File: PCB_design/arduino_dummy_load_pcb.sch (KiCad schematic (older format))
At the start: 22 parts, among them J1 Barrel_Jack, J2 Conn_02x08_Odd_Even, U1 MCP3208

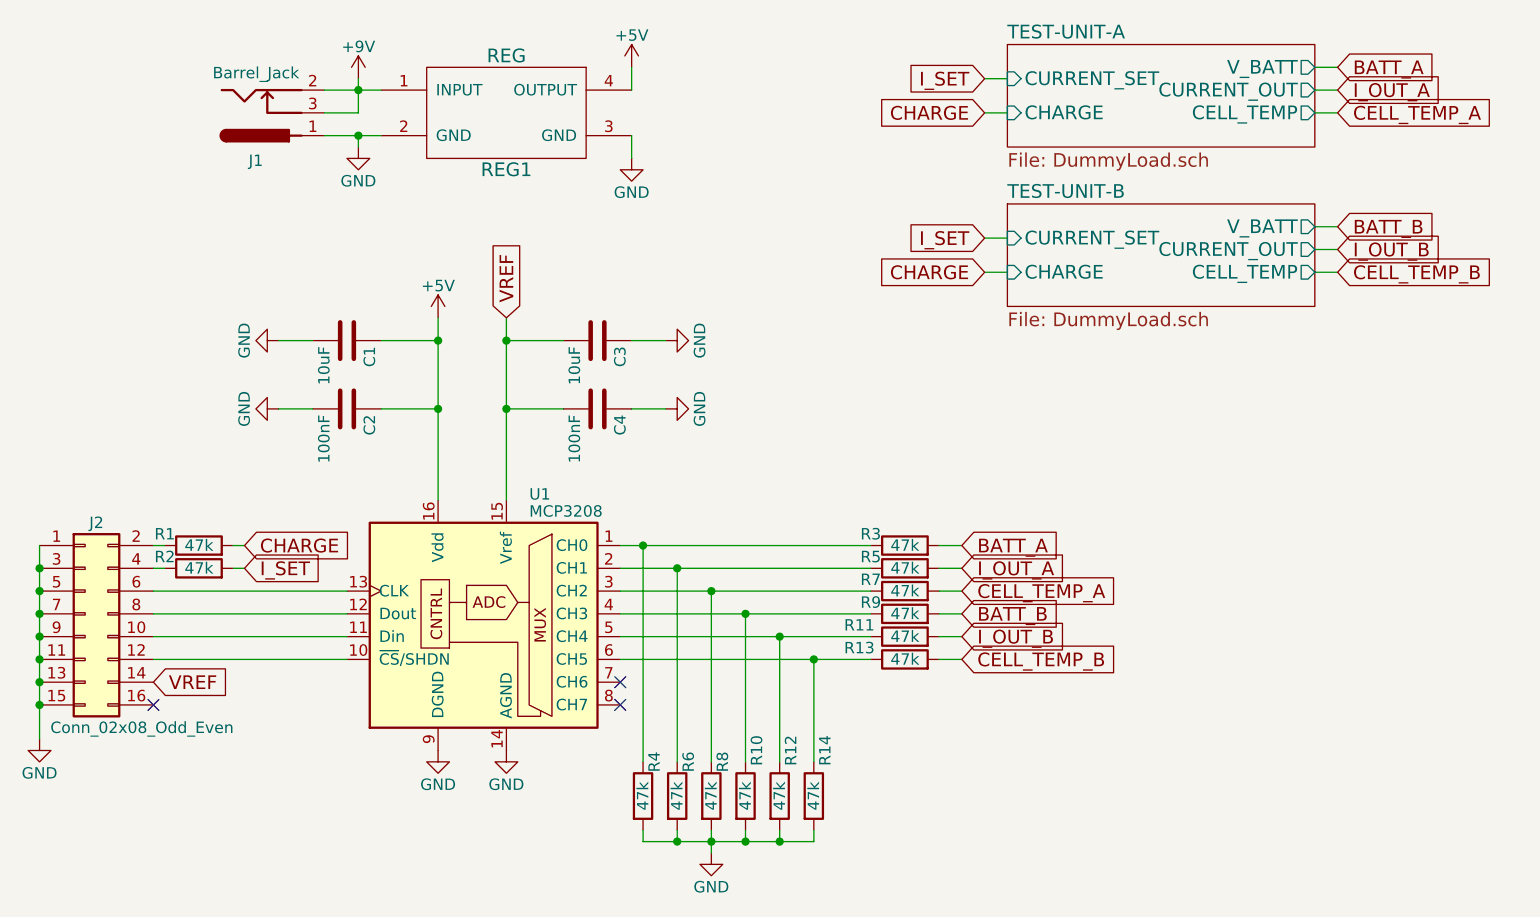
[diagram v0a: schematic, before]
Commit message: nearly finished PCB layout and routing
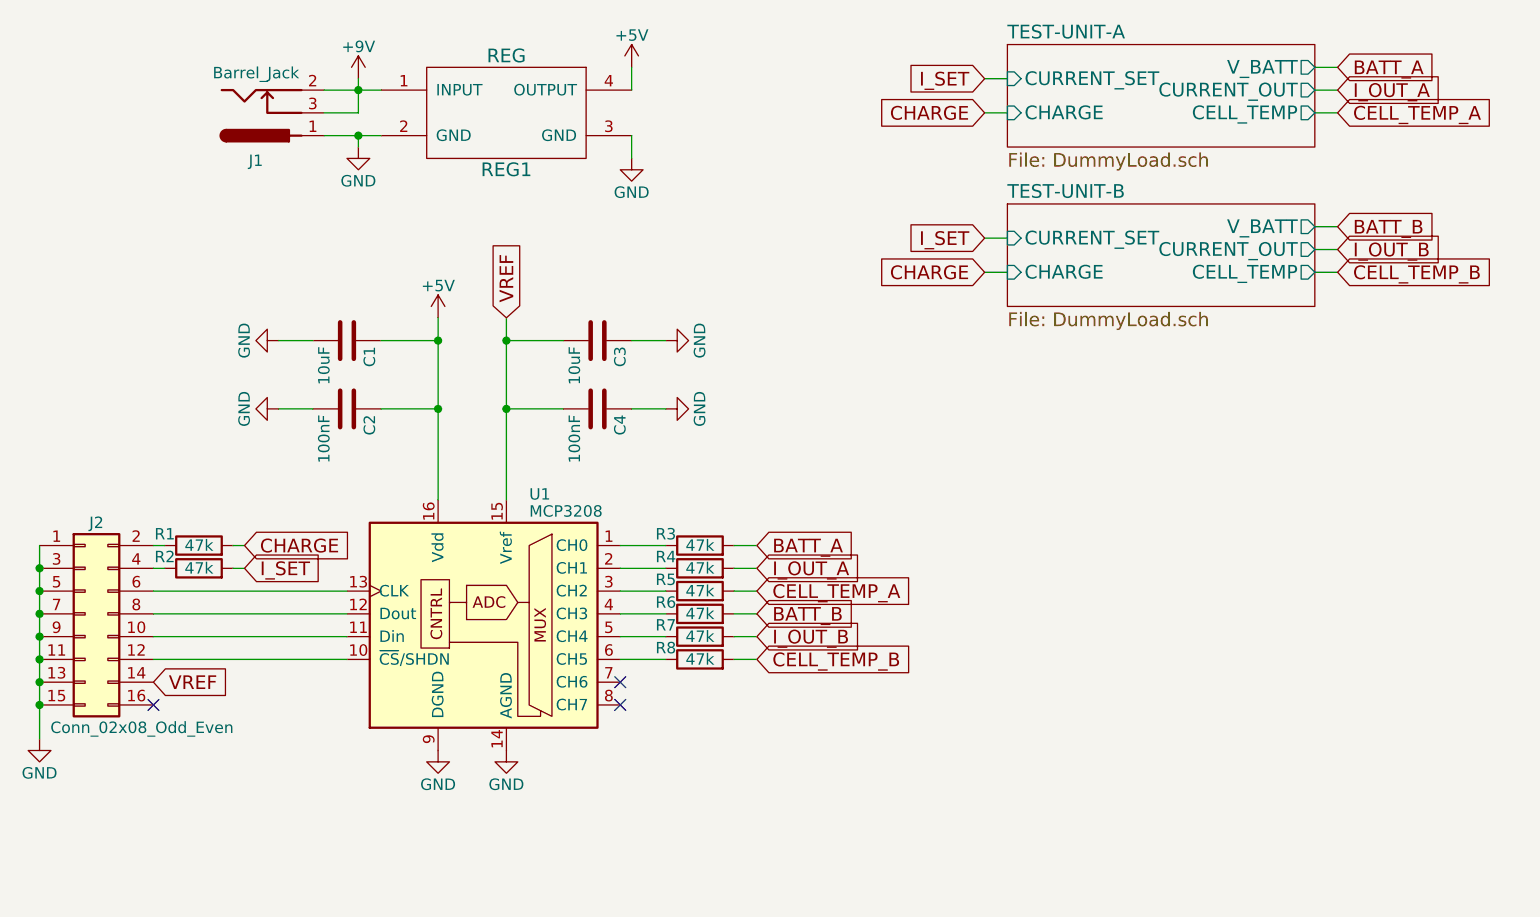
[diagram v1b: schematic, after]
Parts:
- removed R10, R11, R12, R13, R14, R9: 47k, Resistors_SMD:R_0805_HandSoldering, symbol R
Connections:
- net BATT_B: now also R6.2
- net CELL_TEMP_A: now also R5.2; no longer R7.2
- net CELL_TEMP_B: now also R8.2
- net GND: no longer R4.2, R6.2, R8.2
- net I_OUT_A: now also R4.2; no longer R5.2
- net I_OUT_B: now also R7.2
- net at R3.1, U1.1 (CH0): no longer R4.1
- net at U1.4 (CH3): now also R6.1
- net at U1.5 (CH4): now also R7.1
- net at U1.6 (CH5): now also R8.1
- new net: R4.1, U1.2 (CH1)
- new net: R5.1, U1.3 (CH2)
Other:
- moved on the sheet: R3, R4, R5, R6, R7, R8

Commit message: Finalized/finished PCB layout. Phew! Version 0.00. Hopefully it works (fingers crossed)!
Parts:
- removed R8: 47k, Resistors_SMD:R_0805_HandSoldering, symbol R
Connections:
- net BATT_B: now also R5.2; no longer R6.2
- net CELL_TEMP_A: now also R4.2; no longer R5.2
- net CELL_TEMP_B: now also R7.2
- net I_OUT_A: now also U1.2 (CH1); no longer R4.2
- net I_OUT_B: now also R6.2; no longer R7.2
- net at R4.1: now also U1.3 (CH2); no longer U1.2 (CH1)
- net at R5.1: now also U1.4 (CH3); no longer U1.3 (CH2)
- net at R6.1: now also U1.5 (CH4); no longer U1.4 (CH3)
- net at R7.1: now also U1.6 (CH5); no longer U1.5 (CH4)
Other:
- moved on the sheet: R4, R5, R6, R7
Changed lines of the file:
@@
 L R R4
 U 1 1 5A216AEF
-P 4500 3250
-F 0 "R4" V 4550 3400 50  0000 C CNN
-F 1 "47k" V 4500 3250 50  0000 C CNN
-F 2 "Resistors_SMD:R_0805_HandSoldering" V 4430 3250 50  0001 C CNN
-F 3 "" H 4500 3250 50  0001 C CNN
-	1    4500 3250
-	0    -1   -1   0
-$EndComp
-Text GLabel 2500 3150 2    60   Input ~ 0
-CHARGE
-$Comp
-L R R5
-U 1 1 5A22131E
 P 4500 3350
-F 0 "R5" V 4550 3500 50  0000 C CNN
+F 0 "R4" V 4550 3500 50  0000 C CNN
 F 1 "47k" V 4500 3350 50  0000 C CNN
 F 2 "Resistors_SMD:R_0805_HandSoldering" V 4430 3350 50  0001 C CNN
@@
 	0    -1   -1   0
 $EndComp
+Text GLabel 2500 3150 2    60   Input ~ 0
+CHARGE
+$Comp
+L R R5
+U 1 1 5A22131E
+P 4500 3450
+F 0 "R5" V 4550 3600 50  0000 C CNN
+F 1 "47k" V 4500 3450 50  0000 C CNN
+F 2 "Resistors_SMD:R_0805_HandSoldering" V 4430 3450 50  0001 C CNN
+F 3 "" H 4500 3450 50  0001 C CNN
+	1    4500 3450
+	0    -1   -1   0
+$EndComp
 $Comp
 L R R7
 U 1 1 5A22951F
+P 4500 3650
+F 0 "R7" V 4550 3800 50  0000 C CNN
+F 1 "47k" V 4500 3650 50  0000 C CNN
+F 2 "Resistors_SMD:R_0805_HandSoldering" V 4430 3650 50  0001 C CNN
+F 3 "" H 4500 3650 50  0001 C CNN
+	1    4500 3650
+	0    -1   -1   0
+$EndComp
+$Comp
+L R R6
+U 1 1 5A2293D0
 P 4500 3550
-F 0 "R7" V 4550 3700 50  0000 C CNN
+F 0 "R6" V 4550 3700 50  0000 C CNN
 F 1 "47k" V 4500 3550 50  0000 C CNN
 F 2 "Resistors_SMD:R_0805_HandSoldering" V 4430 3550 50  0001 C CNN
@@
 	0    -1   -1   0
 $EndComp
-$Comp
-L R R6
-U 1 1 5A2293D0
-P 4500 3450
-F 0 "R6" V 4550 3600 50  0000 C CNN
-F 1 "47k" V 4500 3450 50  0000 C CNN
-F 2 "Resistors_SMD:R_0805_HandSoldering" V 4430 3450 50  0001 C CNN
-F 3 "" H 4500 3450 50  0001 C CNN
-	1    4500 3450
-	0    -1   -1   0
-$EndComp
 Text GLabel 4750 3350 2    60   Input ~ 0
 CELL_TEMP_A
 Text GLabel 4750 3650 2    60   Input ~ 0
 CELL_TEMP_B
-$Comp
-L R R8
-U 1 1 5A230070
-P 4500 3650
-F 0 "R8" V 4550 3800 50  0000 C CNN
-F 1 "47k" V 4500 3650 50  0000 C CNN
-F 2 "Resistors_SMD:R_0805_HandSoldering" V 4430 3650 50  0001 C CNN
-F 3 "" H 4500 3650 50  0001 C CNN
-	1    4500 3650
-	0    -1   -1   0
-$EndComp
 $Comp
 L Conn_02x08_Odd_Even J2
@@
 $EndComp
 $Comp
-L +5V #PWR07
+L +5V #PWR06
 U 1 1 59F7FE3E
 P 3350 2150
-F 0 "#PWR07" H 3350 2000 50  0001 C CNN
+F 0 "#PWR06" H 3350 2000 50  0001 C CNN
 F 1 "+5V" H 3350 2290 50  0000 C CNN
 F 2 "" H 3350 2150 50  0001 C CNN
@@
 $EndComp
 $Comp
-L GND #PWR08
+L GND #PWR07
 U 1 1 59F80B3F
 P 3350 4050
-F 0 "#PWR08" H 3350 3800 50  0001 C CNN
+F 0 "#PWR07" H 3350 3800 50  0001 C CNN
 F 1 "GND" H 3350 3900 50  0000 C CNN
 F 2 "" H 3350 4050 50  0001 C CNN
@@
 $EndComp
 $Comp
-L GND #PWR09
+L GND #PWR08
 U 1 1 59F80CA3
 P 2650 2250
-F 0 "#PWR09" H 2650 2000 50  0001 C CNN
+F 0 "#PWR08" H 2650 2000 50  0001 C CNN
 F 1 "GND" H 2650 2100 50  0000 C CNN
 F 2 "" H 2650 2250 50  0001 C CNN
@@
 $EndComp
 $Comp
-L GND #PWR010
+L GND #PWR09
 U 1 1 59FD1D7D
 P 4200 1450
-F 0 "#PWR010" H 4200 1200 50  0001 C CNN
+F 0 "#PWR09" H 4200 1200 50  0001 C CNN
 F 1 "GND" H 4200 1300 50  0000 C CNN
 F 2 "" H 4200 1450 50  0001 C CNN
@@
 $EndComp
 Wire Wire Line
-	3000 1100 3000 1150
-Wire Wire Line
-	3000 1150 3000 1250
+	3000 1100 3000 1250
 Wire Wire Line
 	3000 1250 2850 1250
@@
 	4650 3150 4750 3150
 Wire Wire Line
-	4650 3250 4750 3250
+	4150 3250 4750 3250
 Wire Wire Line
 	4200 1350 4200 1450
@@
 	4650 3350 4750 3350
 Wire Wire Line
-	1600 3150 1600 3250
-Wire Wire Line
-	1600 3250 1600 3350
-Wire Wire Line
-	1600 3350 1600 3450
-Wire Wire Line
-	1600 3450 1600 3550
-Wire Wire Line
-	1600 3550 1600 3650
-Wire Wire Line
-	1600 3650 1600 3750
-Wire Wire Line
-	1600 3750 1600 3850
-Wire Wire Line
-	1600 3850 1600 4000
+	1600 3150 1600 4000
 Wire Wire Line
 	2450 3150 2500 3150
@@
 	4150 3350 4350 3350
 Wire Wire Line
-	4150 3250 4350 3250
-Wire Wire Line
-	3350 2150 3350 2250
-Wire Wire Line
-	3350 2250 3350 2550
-Wire Wire Line
-	3350 2550 3350 2950
+	3350 2150 3350 2950
 Wire Wire Line
 	3100 2250 3350 2250
@@
 Connection ~ 3000 1350
 Wire Wire Line
-	2850 1150 3000 1150
-Wire Wire Line
-	3000 1150 3100 1150
-Wire Wire Line
-	2850 1350 3000 1350
-Wire Wire Line
-	3000 1350 3100 1350
+	2850 1150 3100 1150
+Wire Wire Line
+	2850 1350 3100 1350
 Wire Wire Line
 	2100 3150 2150 3150
@@
 VREF
 Wire Wire Line
-	3650 2150 3650 2250
-Wire Wire Line
-	3650 2250 3650 2550
-Wire Wire Line
-	3650 2550 3650 2950
+	3650 2150 3650 2950
 $Comp
 L C C2
@@
 Connection ~ 3650 2550
 $Comp
-L GND #PWR011
+L GND #PWR010
 U 1 1 5A04B5B5
 P 2650 2550
-F 0 "#PWR011" H 2650 2300 50  0001 C CNN
+F 0 "#PWR010" H 2650 2300 50  0001 C CNN
 F 1 "GND" H 2650 2400 50  0000 C CNN
 F 2 "" H 2650 2550 50  0001 C CNN
@@
 $EndComp
 $Comp
-L GND #PWR012
+L GND #PWR011
 U 1 1 5A04C217
 P 4350 2250
-F 0 "#PWR012" H 4350 2000 50  0001 C CNN
+F 0 "#PWR011" H 4350 2000 50  0001 C CNN
 F 1 "GND" H 4350 2100 50  0000 C CNN
 F 2 "" H 4350 2250 50  0001 C CNN
@@
 	3900 2550 3650 2550
 $Comp
-L GND #PWR013
+L GND #PWR012
 U 1 1 5A04CF95
 P 4350 2550
-F 0 "#PWR013" H 4350 2300 50  0001 C CNN
+F 0 "#PWR012" H 4350 2300 50  0001 C CNN
 F 1 "GND" H 4350 2400 50  0000 C CNN
 F 2 "" H 4350 2550 50  0001 C CNN
